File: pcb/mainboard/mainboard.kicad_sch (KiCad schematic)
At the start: 56 parts, among them J1 V_IN, J3 Control Board, J4 M1, J5 M2, J7 TIP, K1 SANYOU_SRD_Form_C, Q1 NMOS, Q2 NMOS, U2 TPS54331DDA, U3 TMC2208_SILENTSTEPSTICK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

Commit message: Update PCB | Requested Changes
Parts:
- added JP1, JP2, JP3: SolderJumper_2_Open, Jumper:SolderJumper-2_P1.3mm_Open_TrianglePad1.0x1.5mm, symbol Jumper:SolderJumper_2_Open
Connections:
- net +5V: now also JP1.2 (B), JP2.1 (A), JP3.1 (A); no longer C19.1, C20.1, C25.1, L1.2, R10.1, R12.1, R7.2, R9.1, U5.5 (VS), U6.1 (VCC), U6.2 (VCC), U6.32 (VREF+)
- new net BUCK_5V_OUT: C19.1, C20.1, JP1.1 (A), L1.2, R12.1, R7.2
- new net INA_VIN: C25.1, JP3.2 (B), R10.1, R9.1, U5.5 (VS)
- new net uC_VCC: JP2.2 (B), U6.1 (VCC), U6.2 (VCC), U6.32 (VREF+)
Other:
- moved on the sheet: C25

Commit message: Change OLED Connector Size
Changed size of an OLED connector from 2.54mm to 2.00mm to match its size from other related project.
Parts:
- J3: footprint Connector_PinSocket_2.54mm:PinSocket_1x10_P2.54mm_Vertical -> Connector_PinSocket_2.00mm:PinSocket_1x10_P2.00mm_Vertical
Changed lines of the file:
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@@
 			)
 		)
-		(property "Footprint" "Connector_PinSocket_2.54mm:PinSocket_1x10_P2.54mm_Vertical"
+		(property "Footprint" "Connector_PinSocket_2.00mm:PinSocket_1x10_P2.00mm_Vertical"
 			(at 149.86 53.34 0)
 			(effects

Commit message: Add Limit Switches
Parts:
- added J2, J6: Conn_01x02, Connector_PinSocket_2.54mm:PinSocket_1x02_P2.54mm_Vertical, symbol Connector_Generic:Conn_01x02
- added R20, R6: 10k, Resistor_SMD:R_0603_1608Metric_Pad0.98x0.95mm_HandSolder, symbol Device:R
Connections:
- net +3.3V: now also R20.1, R6.1
- net GND: now also J2.2 (Pin_2), J6.2 (Pin_2)
- net LIMIT_SWITCH_1: now reaches U6.29 (PB10)
- net LIMIT_SWITCH_1: now also J2.1 (Pin_1), R6.2
- net LIMIT_SWITCH_2: now reaches U6.31 (PB2)
- net LIMIT_SWITCH_2: now also J6.1 (Pin_1), R20.2
- no-connect marks 28 -> 26
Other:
- note added: "Limit Switches"

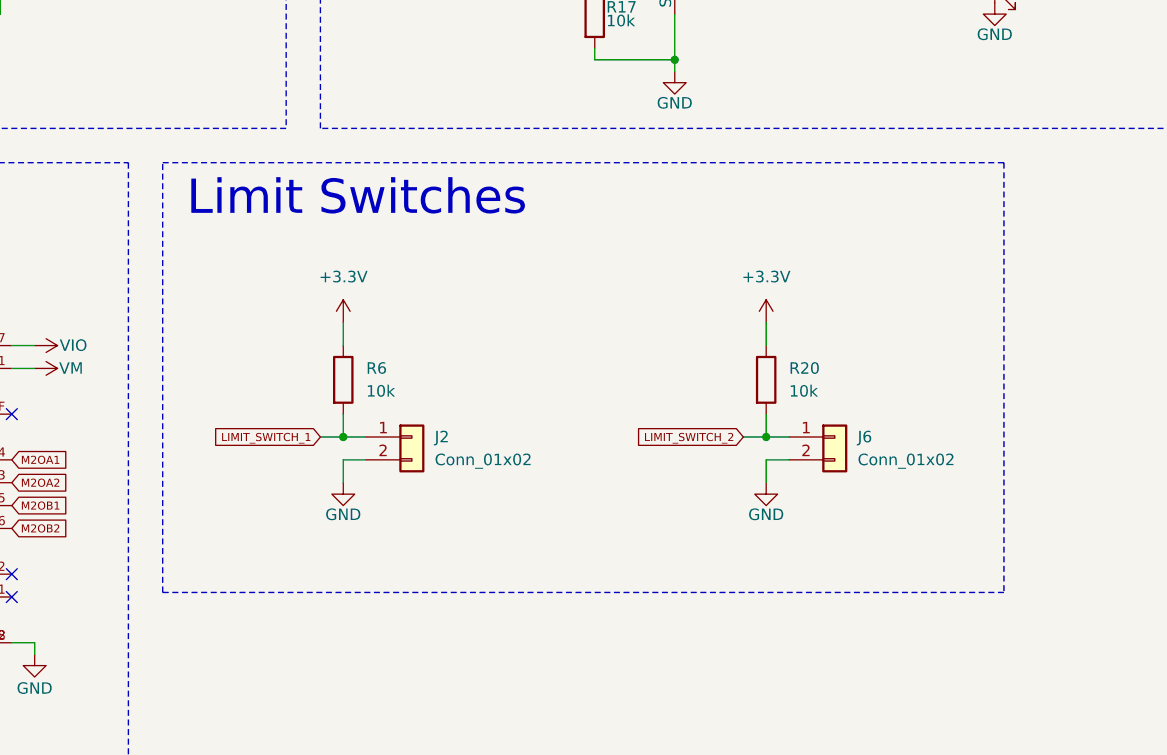
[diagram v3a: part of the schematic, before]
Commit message: Change Limit Switch Connectors
Change from 2 pin to 3 pin connectors
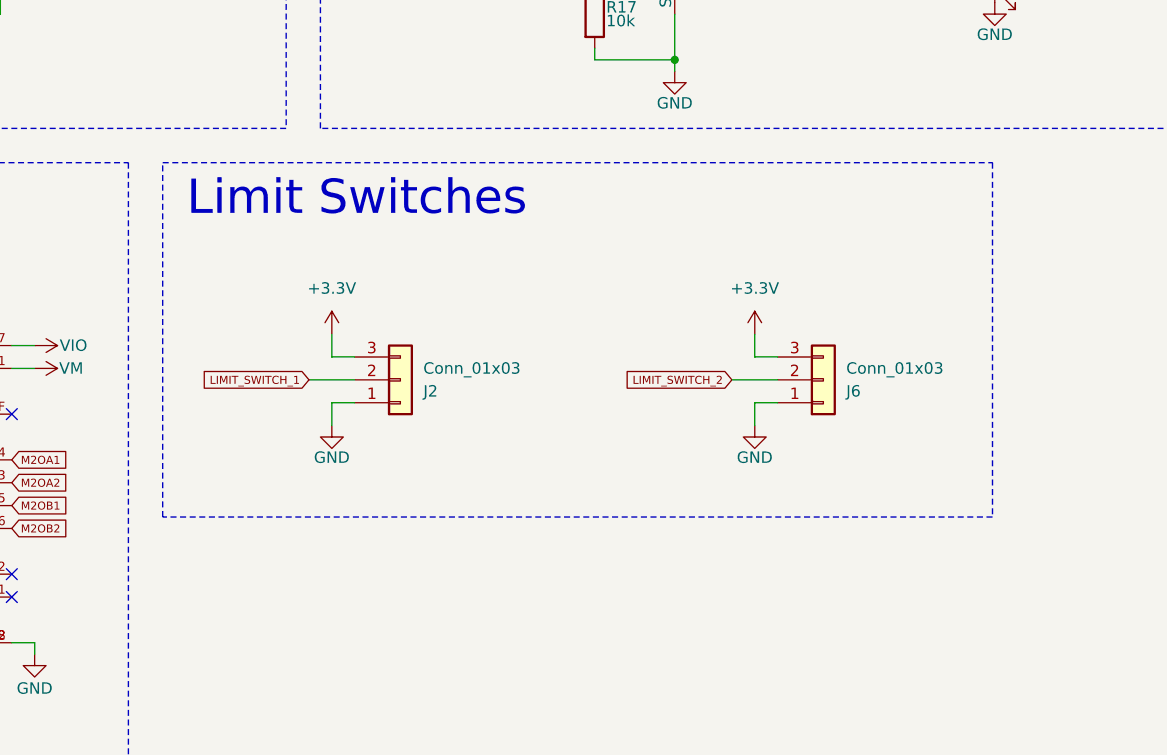
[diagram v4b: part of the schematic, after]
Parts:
- removed J2, J6: Conn_01x02, Connector_PinSocket_2.54mm:PinSocket_1x02_P2.54mm_Vertical, symbol Connector_Generic:Conn_01x02
- removed R20, R6: 10k, Resistor_SMD:R_0603_1608Metric_Pad0.98x0.95mm_HandSolder, symbol Device:R
- added J2, J6: Conn_01x03, Connector_PinSocket_2.54mm:PinSocket_1x03_P2.54mm_Vertical, symbol Connector_Generic:Conn_01x03
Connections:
- net +3.3V: now also J2.3 (Pin_3), J6.3 (Pin_3)
- net GND: now also J2.1 (Pin_1), J6.1 (Pin_1)
- net LIMIT_SWITCH_1: now also J2.2 (Pin_2)
- net LIMIT_SWITCH_2: now also J6.2 (Pin_2)
